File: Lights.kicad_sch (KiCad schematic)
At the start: 10 parts, among them Q1 2N7002, Q2 2N7002, U2 EL3H7, U3 EL3H7

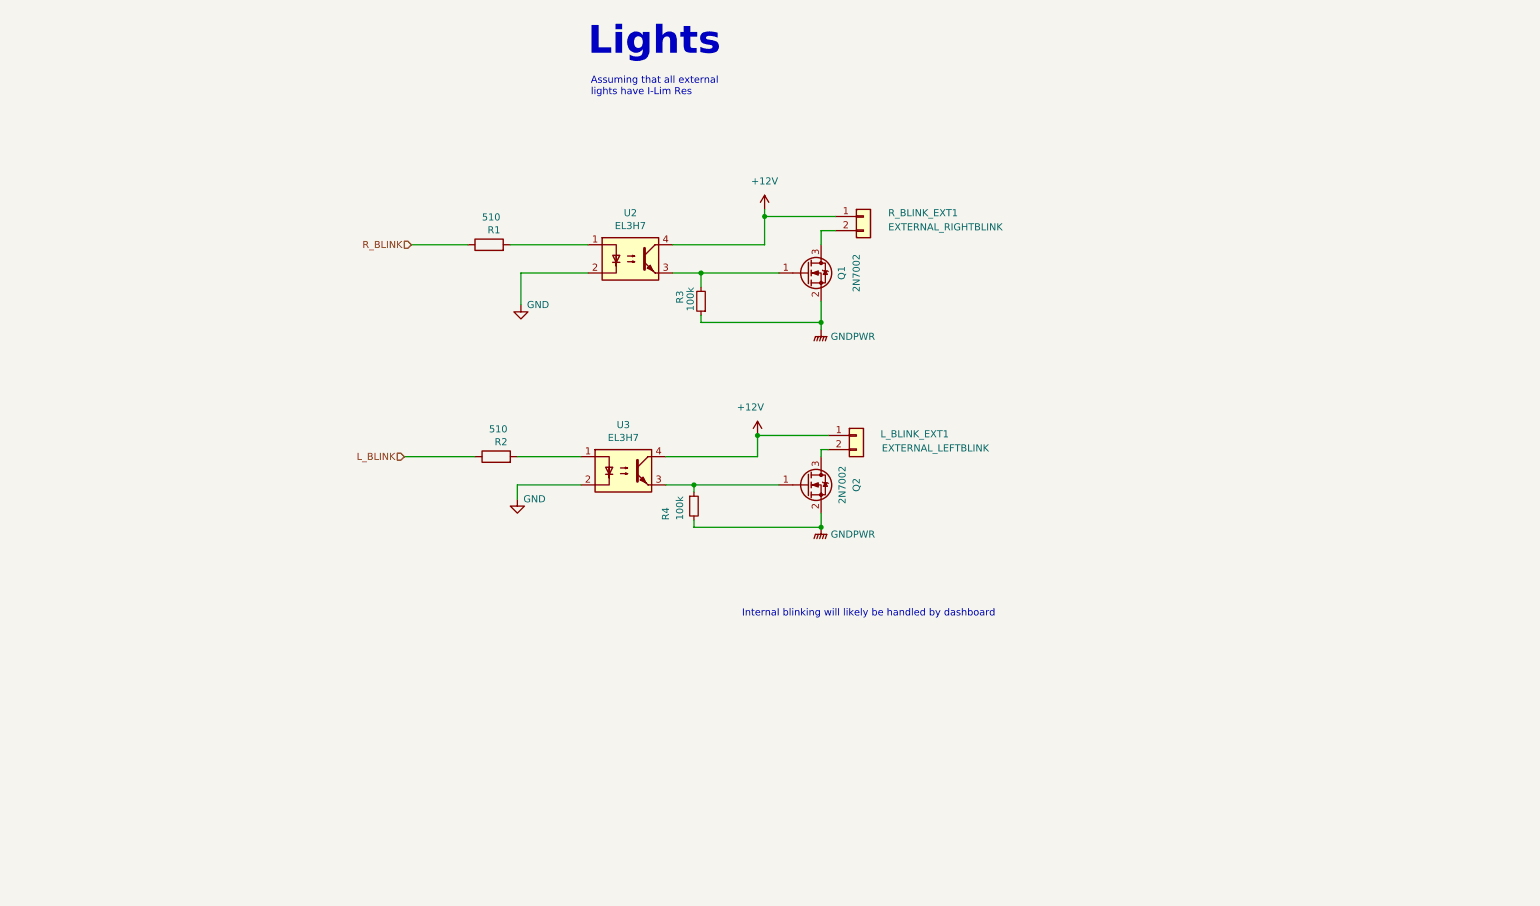
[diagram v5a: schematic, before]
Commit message: accommodated for 6 lights on one board, added test points and leds on board
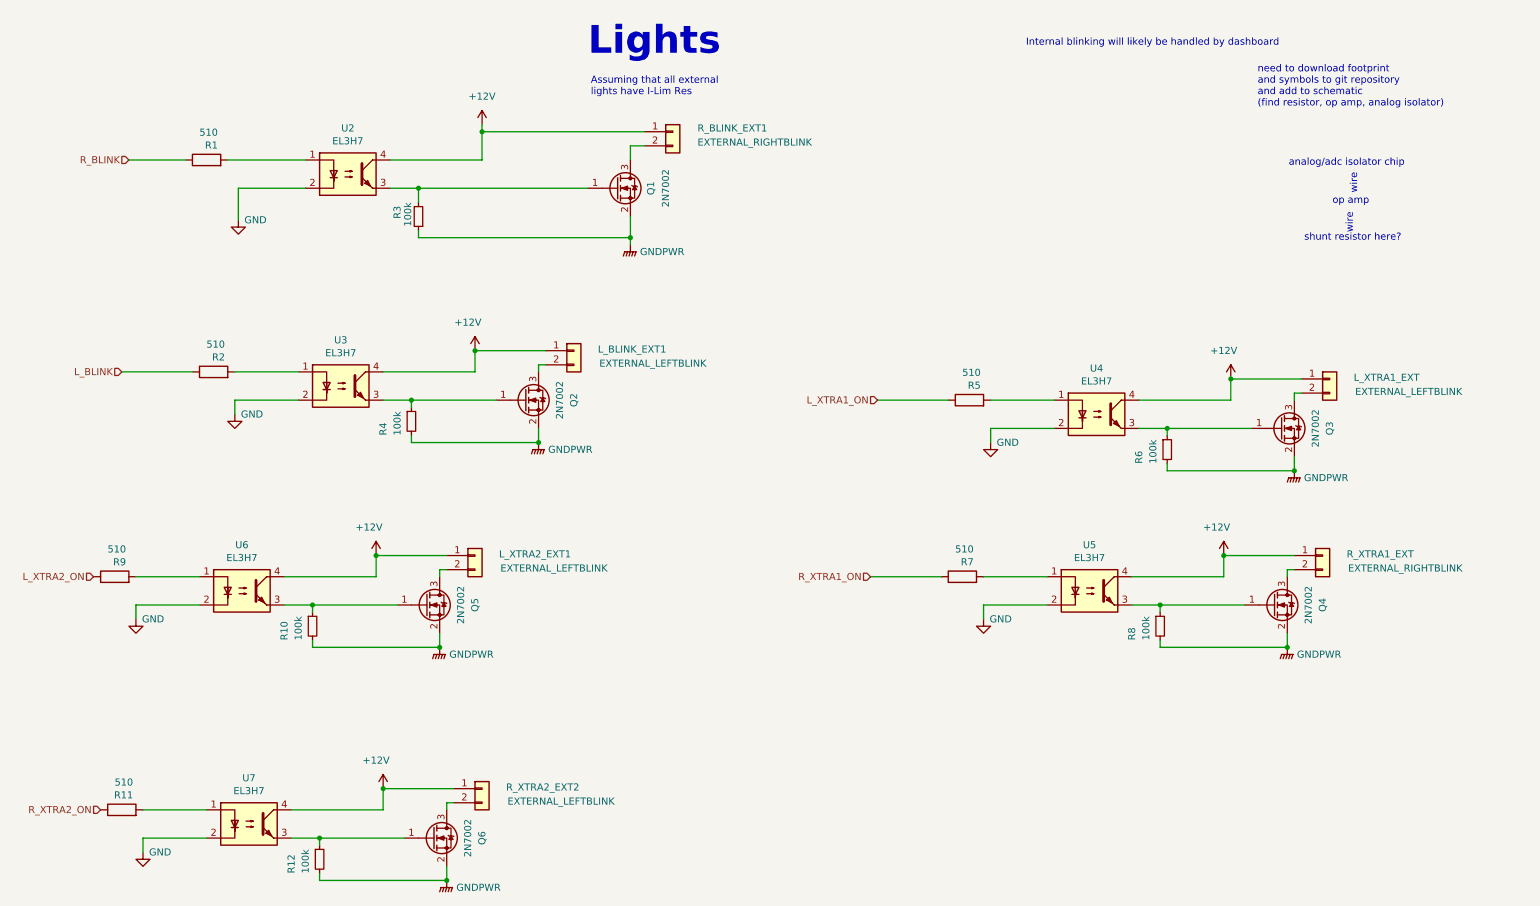
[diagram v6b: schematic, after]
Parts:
- added L_XTRA1_EXT, L_XTRA2_EXT1, R_XTRA2_EXT2: EXTERNAL_LEFTBLINK, Connector_Molex:Molex_Micro-Fit_3.0_43650-0215_1x02_P3.00mm_Vertical, symbol Connector_Generic:Conn_01x02
- added Q3, Q4, Q5, Q6: 2N7002, Package_TO_SOT_SMD:SOT-23, symbol Transistor_FET:2N7002
- added R10, R12, R6, R8: 100k, Resistor_SMD:R_0805_2012Metric, symbol Device:R_Small
- added R11, R5, R7, R9: 510, Resistor_SMD:R_0805_2012Metric, symbol Device:R
- added R_XTRA1_EXT: EXTERNAL_RIGHTBLINK, Connector_Molex:Molex_Micro-Fit_3.0_43650-0215_1x02_P3.00mm_Vertical, symbol Connector_Generic:Conn_01x02
- added U4, U5, U6, U7: EL3H7, Package_DIP:DIP-4_W7.62mm, symbol Isolator:SFH617A-1
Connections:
- net +12V: now also L_XTRA1_EXT.1 (Pin_1), L_XTRA2_EXT1.1 (Pin_1), R_XTRA1_EXT.1 (Pin_1), R_XTRA2_EXT2.1 (Pin_1), U4.4, U5.4, U6.4, U7.4
- net GND: now also U4.2, U5.2, U6.2, U7.2
- net GNDPWR: now also Q3.2 (S), Q4.2 (S), Q5.2 (S), Q6.2 (S), R10.2, R12.2, R6.2, R8.2
- new net: Q5.1 (G), R10.1, U6.3
- new net: L_XTRA2_EXT1.2 (Pin_2), Q5.3 (D)
- new net: Q6.3 (D), R_XTRA2_EXT2.2 (Pin_2)
- new net: Q4.1 (G), R8.1, U5.3
- new net: R7.2, U5.1
- new net: R9.2, U6.1
- new net: Q6.1 (G), R12.1, U7.3
- new net: Q4.3 (D), R_XTRA1_EXT.2 (Pin_2)
- new net: R11.2, U7.1
- new net: Q3.1 (G), R6.1, U4.3
- new net: L_XTRA1_EXT.2 (Pin_2), Q3.3 (D)
- new net: R5.2, U4.1
- new net L_XTRA1_ON: R5.1
- new net L_XTRA2_ON: R9.1
- new net R_XTRA1_ON: R7.1
- new net R_XTRA2_ON: R11.1
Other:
- note added: "analog/adc isolator chip"
- note added: "need to download footprint and symbols to git repository and add to schematic (find resistor, op amp, analog isolator)"
- note added: "op amp"
- note added: "shunt resistor here?"
- note added: "wire"
- moved on the sheet: L_BLINK_EXT1, Q1, Q2, R1, R2, R3, R4, R_BLINK_EXT1, U2, U3

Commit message: changed lights resistor values and updated EL2H7 footprint
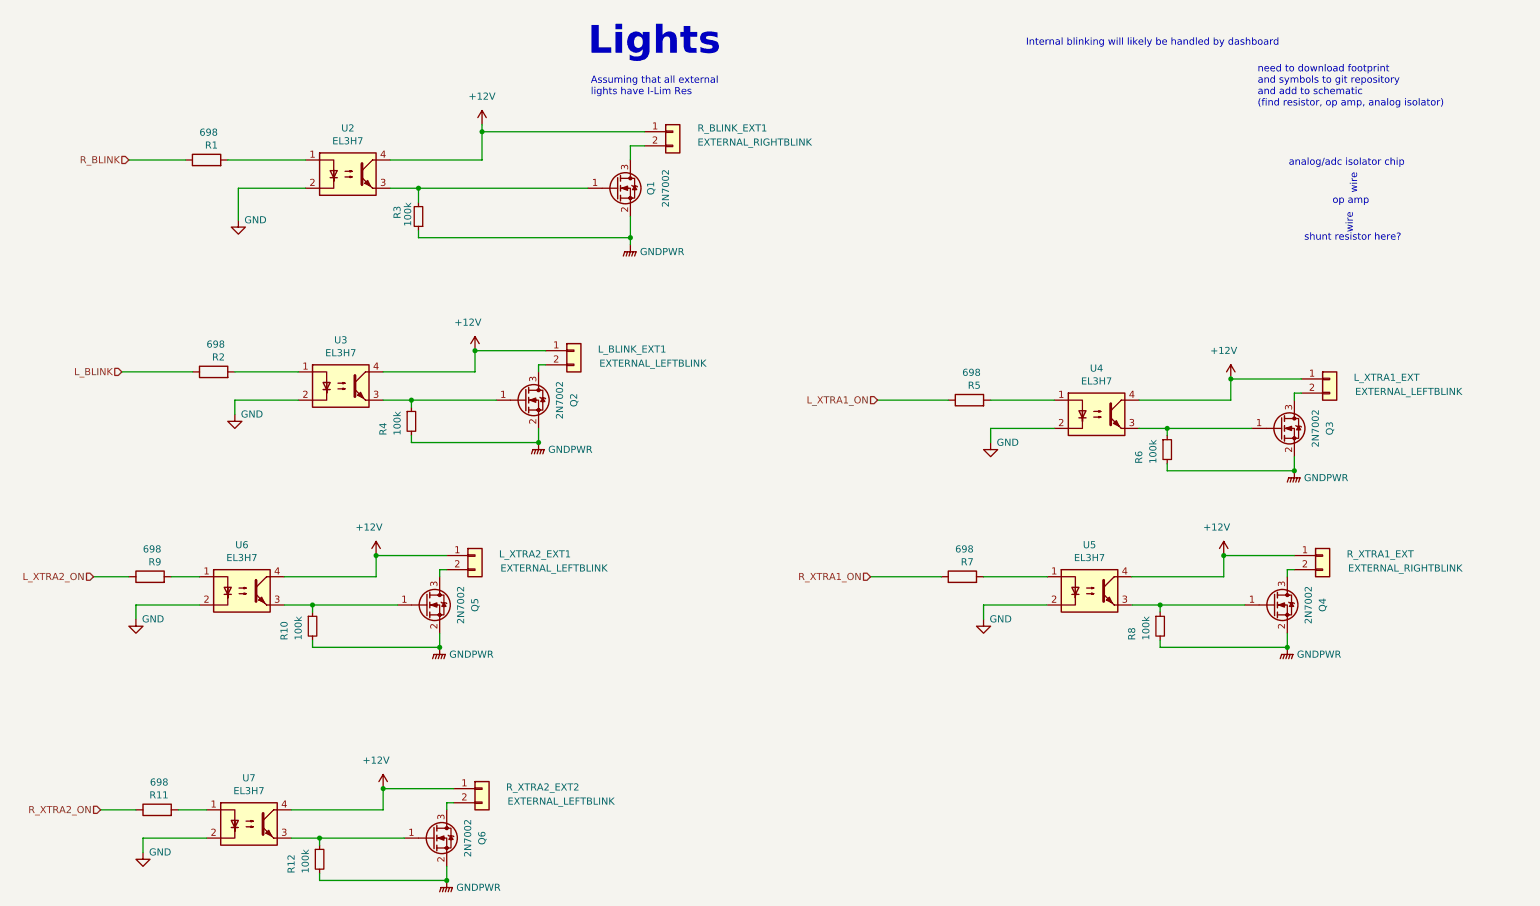
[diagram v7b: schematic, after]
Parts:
- R1, R11, R2, R5, R7, R9: value 510 -> 698
- U2, U3, U4, U5, U6, U7: footprint Package_DIP:DIP-4_W7.62mm -> Package_SO:SSOP-4_4.4x2.6mm_P1.27mm
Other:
- moved on the sheet: R11, R9
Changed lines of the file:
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@@
 	(wire
 		(pts
+			(xy 36.83 130.81) (xy 30.48 130.81)
+		)
+		(stroke
+			(width 0)
+			(type default)
+		)
+	)
+	(wire
+		(pts
 			(xy 69.85 135.89) (xy 69.85 137.16)
 		)
@@
 	(wire
 		(pts
-			(xy 38.1 130.81) (xy 49.53 130.81)
+			(xy 44.45 130.81) (xy 49.53 130.81)
 		)
 		(stroke
@@
 	(wire
 		(pts
+			(xy 38.1 172.72) (xy 31.75 172.72)
+		)
+		(stroke
+			(width 0)
+			(type default)
+		)
+	)
+	(wire
+		(pts
 			(xy 92.71 129.54) (xy 92.71 130.81)
 		)
@@
 	(wire
 		(pts
-			(xy 39.37 172.72) (xy 50.8 172.72)
+			(xy 45.72 172.72) (xy 50.8 172.72)
 		)
 		(stroke
@@
 			)
 		)
-		(property "Footprint" "Package_DIP:DIP-4_W7.62mm"
+		(property "Footprint" "Package_SO:SSOP-4_4.4x2.6mm_P1.27mm"
 			(at 71.12 63.5 0)
 			(effects
@@
 			)
 		)
-		(property "Value" "510"
+		(property "Value" "698"
 			(at 54.102 89.027 90)
 			(effects
@@
 			)
 		)
-		(property "Value" "510"
+		(property "Value" "698"
 			(at 188.722 125.857 90)
 			(effects
@@
 	(symbol
 		(lib_id "Device:R")
-		(at 34.29 130.81 90)
+		(at 40.64 130.81 90)
 		(unit 1)
 		(exclude_from_sim no)
@@
 		(dnp no)
 		(property "Reference" "R9"
-			(at 36.322 128.1684 90)
+			(at 42.672 128.1684 90)
 			(effects
 				(font
@@
 			)
 		)
-		(property "Value" "510"
-			(at 36.322 125.857 90)
+		(property "Value" "698"
+			(at 42.672 125.857 90)
 			(effects
 				(font
@@
 		)
 		(property "Footprint" "Resistor_SMD:R_0805_2012Metric"
-			(at 34.29 132.588 90)
+			(at 40.64 132.588 90)
 			(effects
 				(font
@@
 		)
 		(property "Datasheet" "~"
-			(at 34.29 130.81 0)
+			(at 40.64 130.81 0)
 			(effects
 				(font
@@
 		)
 		(property "Description" ""
-			(at 34.29 130.81 0)
+			(at 40.64 130.81 0)
 			(effects
 				(font
@@
 		)
 		(property "P/N" "SDR10EZPJ152"
-			(at 34.29 130.81 90)
+			(at 40.64 130.81 90)
 			(effects
 				(font
@@
 			)
 		)
-		(property "Footprint" "Package_DIP:DIP-4_W7.62mm"
+		(property "Footprint" "Package_SO:SSOP-4_4.4x2.6mm_P1.27mm"
 			(at 53.34 180.34 0)
 			(effects
@@
 			)
 		)
-		(property "Value" "510"
+		(property "Value" "698"
 			(at 52.832 50.927 90)
 			(effects
@@
 			)
 		)
-		(property "Footprint" "Package_DIP:DIP-4_W7.62mm"
+		(property "Footprint" "Package_SO:SSOP-4_4.4x2.6mm_P1.27mm"
 			(at 52.07 138.43 0)
 			(effects
@@
 			)
 		)
-		(property "Footprint" "Package_DIP:DIP-4_W7.62mm"
+		(property "Footprint" "Package_SO:SSOP-4_4.4x2.6mm_P1.27mm"
 			(at 204.47 138.43 0)
 			(effects
@@
 			)
 		)
-		(property "Value" "510"
+		(property "Value" "698"
 			(at 189.992 94.107 90)
 			(effects
@@
 			)
 		)
-		(property "Footprint" "Package_DIP:DIP-4_W7.62mm"
+		(property "Footprint" "Package_SO:SSOP-4_4.4x2.6mm_P1.27mm"
 			(at 69.85 101.6 0)
 			(effects
@@
 	(symbol
 		(lib_id "Device:R")
-		(at 35.56 172.72 90)
+		(at 41.91 172.72 90)
 		(unit 1)
 		(exclude_from_sim no)
@@
 		(dnp no)
 		(property "Reference" "R11"
-			(at 37.592 170.0784 90)
+			(at 43.942 170.0784 90)
 			(effects
 				(font
@@
 			)
 		)
-		(property "Value" "510"
-			(at 37.592 167.767 90)
+		(property "Value" "698"
+			(at 43.942 167.767 90)
 			(effects
 				(font
@@
 		)
 		(property "Footprint" "Resistor_SMD:R_0805_2012Metric"
-			(at 35.56 174.498 90)
+			(at 41.91 174.498 90)
 			(effects
 				(font
@@
 		)
 		(property "Datasheet" "~"
-			(at 35.56 172.72 0)
+			(at 41.91 172.72 0)
 			(effects
 				(font
@@
 		)
 		(property "Description" ""
-			(at 35.56 172.72 0)
+			(at 41.91 172.72 0)
 			(effects
 				(font
@@
 		)
 		(property "P/N" "SDR10EZPJ152"
-			(at 35.56 172.72 90)
+			(at 41.91 172.72 90)
 			(effects
 				(font
@@
 			)
 		)
-		(property "Footprint" "Package_DIP:DIP-4_W7.62mm"
+		(property "Footprint" "Package_SO:SSOP-4_4.4x2.6mm_P1.27mm"
 			(at 205.74 106.68 0)
 			(effects

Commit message: small changes, debating new connectors
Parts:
- added J3: Conn_01x12, symbol Connector_Generic:Conn_01x12
- added J4: Conn_02x06_Odd_Even, symbol Connector_Generic:Conn_02x06_Odd_Even
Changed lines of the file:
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@@
+	)
+	(symbol
+		(lib_id "Connector_Generic:Conn_02x06_Odd_Even")
+		(at 212.09 60.96 0)
+		(unit 1)
+		(exclude_from_sim no)
+		(in_bom yes)
+		(on_board yes)
+		(dnp no)
+		(fields_autoplaced yes)
+		(property "Reference" "J4"
+			(at 213.36 49.53 0)
+			(effects
+				(font
+					(size 1.27 1.27)
+				)
+			)
+		)
+		(property "Value" "Conn_02x06_Odd_Even"
+			(at 213.36 52.07 0)
+			(effects
+				(font
+					(size 1.27 1.27)
+				)
+			)
+		)
+		(property "Footprint" ""
+			(at 212.09 60.96 0)
+			(effects
+				(font
+					(size 1.27 1.27)
+				)
+				(hide yes)
+			)
+		)
+		(property "Datasheet" "~"
+			(at 212.09 60.96 0)
+			(effects
+				(font
+					(size 1.27 1.27)
+				)
+				(hide yes)
+			)
+		)
+		(property "Description" "Generic connector, double row, 02x06, odd/even pin numbering scheme (row 1 odd numbers, row 2 even numbers), script generated (kicad-library-utils/schlib/autogen/connector/)"
+			(at 212.09 60.96 0)
+			(effects
+				(font
+					(size 1.27 1.27)
+				)
+				(hide yes)
+			)
+		)
+		(pin "5"
+		)
+		(pin "1"
+		)
+		(pin "10"
+		)
+		(pin "11"
+		)
+		(pin "9"
+		)
+		(pin "12"
+		)
+		(pin "6"
+		)
+		(pin "8"
+		)
+		(pin "2"
+		)
+		(pin "7"
+		)
+		(pin "4"
+		)
+		(pin "3"
+		)
+		(instances
+			(project ""
+				(path "/229b82f0-5048-47d6-8bc8-0bcee42eb4bc/ceb5a95e-a274-4dea-8a59-96d1af6e854d"
+					(reference "J4")
+					(unit 1)
+				)
+			)
+		)
 	)
 	(symbol
@@
 					(unit 1)
 				)
+			)
+		)
+	)
+	(symbol
+		(lib_id "Connector_Generic:Conn_01x12")
+		(at 173.99 68.58 0)
+		(unit 1)
+		(exclude_from_sim no)
+		(in_bom yes)
+		(on_board yes)
+		(dnp no)
+		(fields_autoplaced yes)
+		(property "Reference" "J3"
+			(at 176.53 68.5799 0)
+			(effects
+				(font
+					(size 1.27 1.27)
+				)
+				(justify left)
+			)
+		)
+		(property "Value" "Conn_01x12"
+			(at 176.53 71.1199 0)
+			(effects
+				(font
+					(size 1.27 1.27)
+				)
+				(justify left)
+			)
+		)
+		(property "Footprint" ""
+			(at 173.99 68.58 0)
+			(effects
+				(font
+					(size 1.27 1.27)
+				)
+				(hide yes)
+			)
+		)
+		(property "Datasheet" "~"
+			(at 173.99 68.58 0)
+			(effects
+				(font
+					(size 1.27 1.27)
+				)
+				(hide yes)
+			)
+		)
+		(property "Description" "Generic connector, single row, 01x12, script generated (kicad-library-utils/schlib/autogen/connector/)"
+			(at 173.99 68.58 0)
+			(effects
+				(font
+					(size 1.27 1.27)
+				)
+				(hide yes)
+			)
+		)
+		(pin "7"
+		)
+		(pin "8"
+		)
+		(pin "10"
+		)
+		(pin "12"
+		)
+		(pin "9"
+		)
+		(pin "2"
+		)
+		(pin "5"
+		)
+		(pin "11"
+		)
+		(pin "6"
+		)
+		(pin "1"
+		)
+		(pin "3"
+		)
+		(pin "4"
+		)
+		(instances
+			(project ""
+				(path "/229b82f0-5048-47d6-8bc8-0bcee42eb4bc/ceb5a95e-a274-4dea-8a59-96d1af6e854d"
+					(reference "J3")
+					(unit 1)
+				)
